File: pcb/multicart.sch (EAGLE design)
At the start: 16 parts, among them IC1 74HCT373N, IC3 27C08032P6, IC5 74HCT08N, Q1 BS170

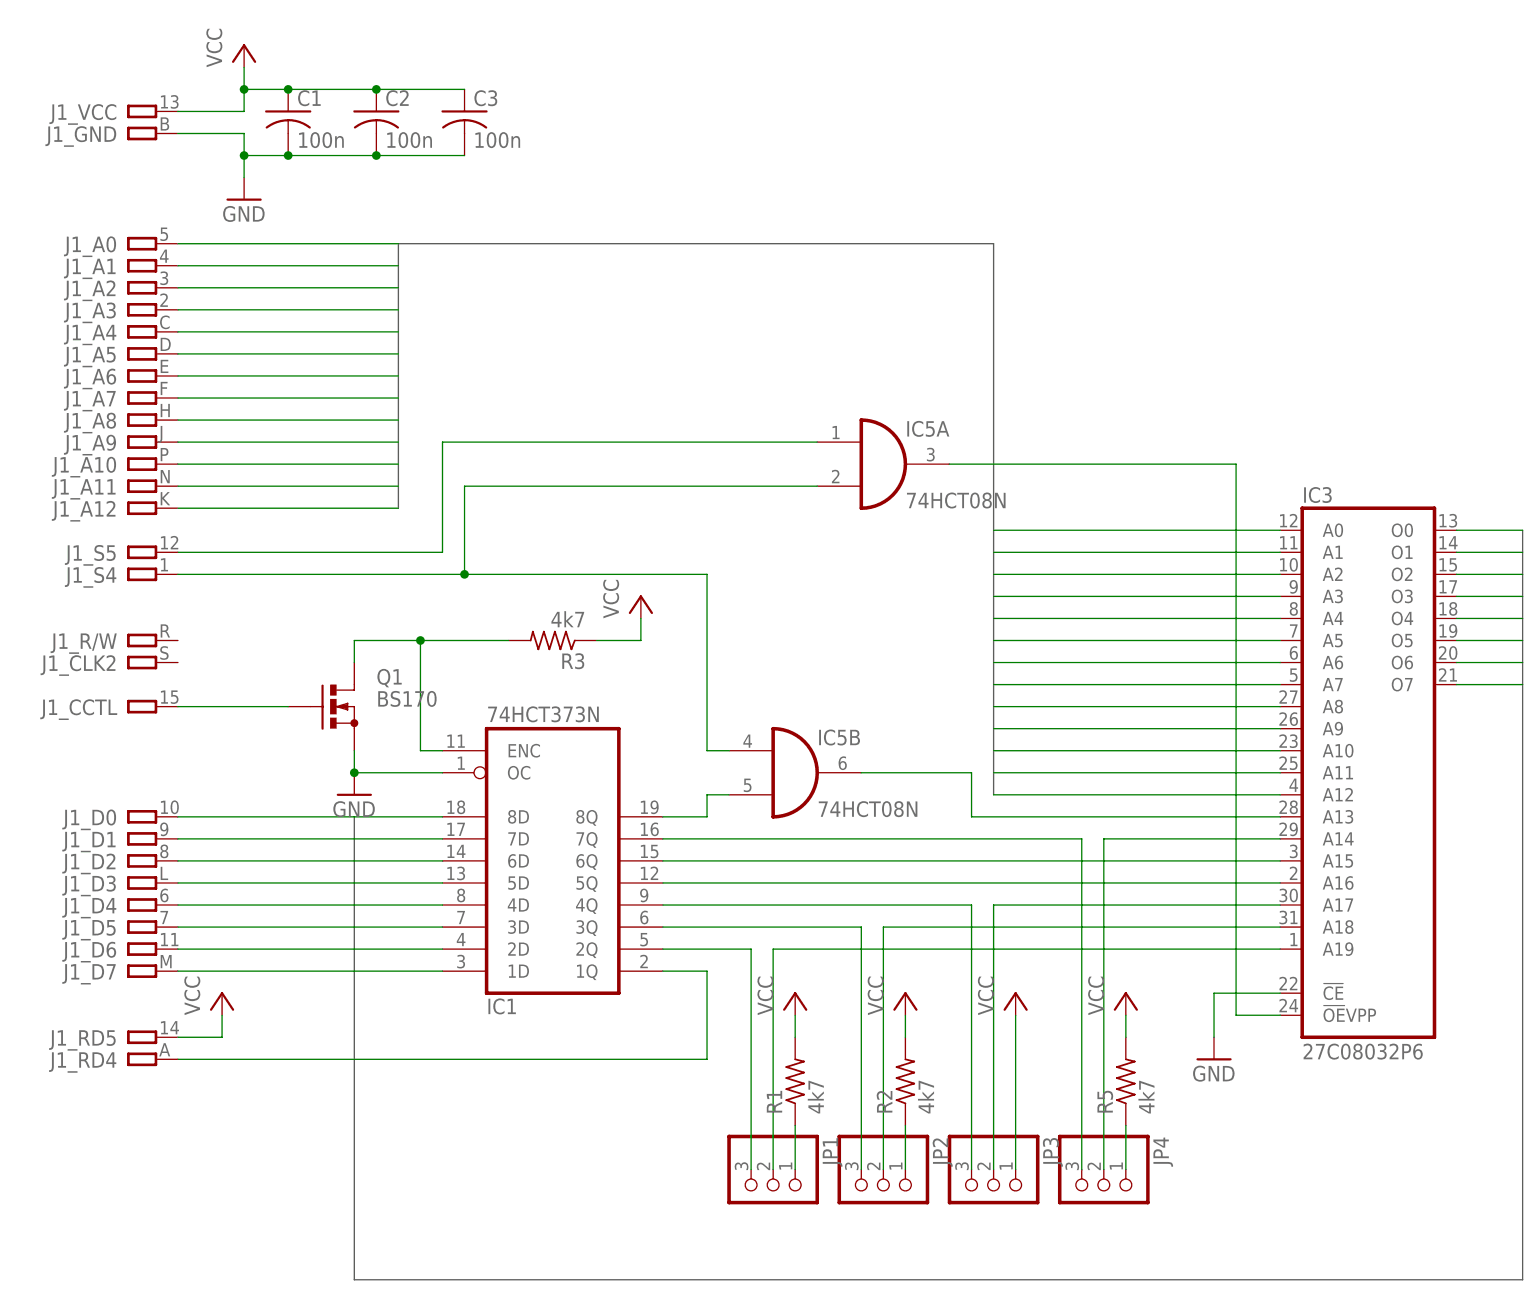
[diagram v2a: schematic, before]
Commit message: Optimized the PCB design.
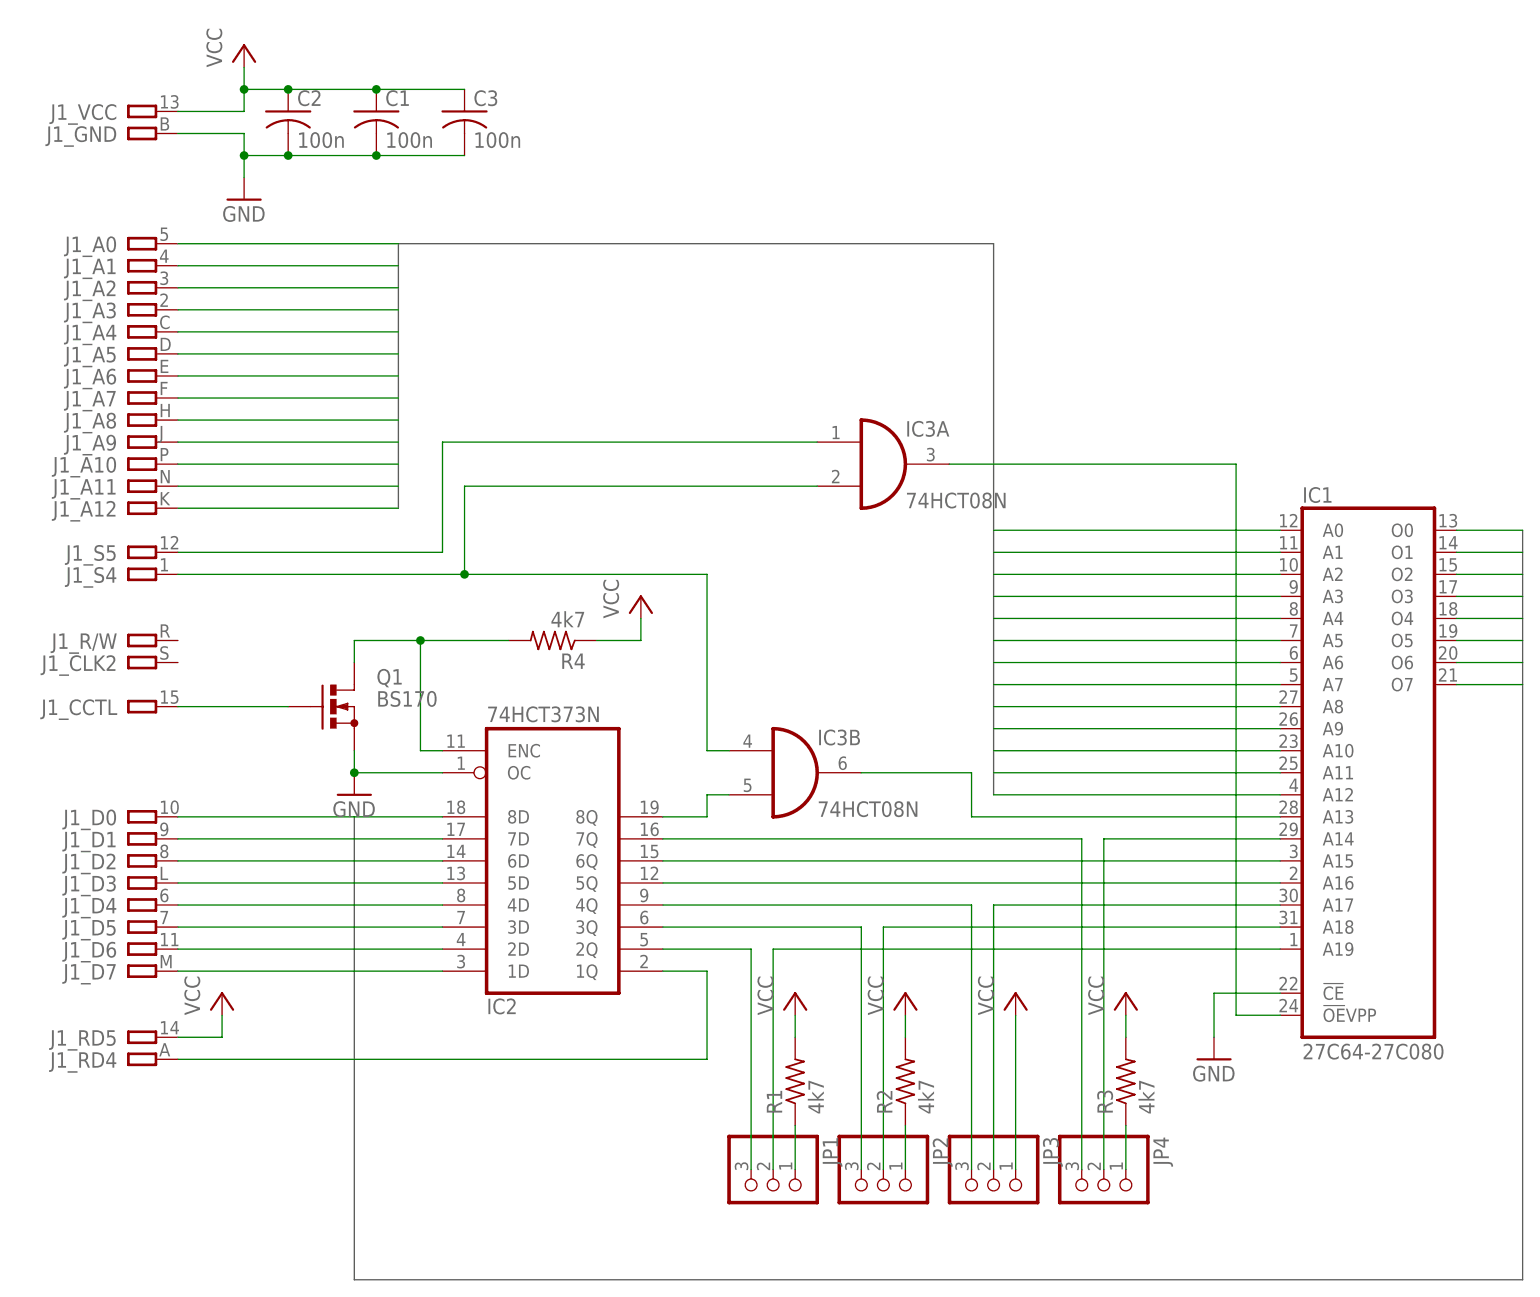
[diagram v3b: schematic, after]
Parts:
- removed IC5: 74HCT08N, 74xx-eu:74HCT08N
- removed R5: 4k7, resistor:R-US_0204/7
- added IC2: 74HCT373N, 74xx-eu:74HCT373N
- added R4: 4k7, resistor:R-US_0204/7
- IC1: value 74HCT373N -> 27C64-27C080; device 74xx-eu:74HCT373N -> atmel:27C08032P6
- IC3: value 27C08032P6 -> 74HCT08N; device atmel:27C08032P6 -> 74xx-eu:74HCT08N
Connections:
- net A0: now also IC1G$1.A0; no longer IC3G$1.A0
- net A1: now also IC1G$1.A1; no longer IC3G$1.A1
- net A10: now also IC1G$1.A10; no longer IC3G$1.A10
- net A11: now also IC1G$1.A11; no longer IC3G$1.A11
- net A12: now also IC1G$1.A12; no longer IC3G$1.A12
- net A2: now also IC1G$1.A2; no longer IC3G$1.A2
- net A3: now also IC1G$1.A3; no longer IC3G$1.A3
- net A4: now also IC1G$1.A4; no longer IC3G$1.A4
- net A5: now also IC1G$1.A5; no longer IC3G$1.A5
- net A6: now also IC1G$1.A6; no longer IC3G$1.A6
- net A7: now also IC1G$1.A7; no longer IC3G$1.A7
- net A8: now also IC1G$1.A8; no longer IC3G$1.A8
- net A9: now also IC1G$1.A9; no longer IC3G$1.A9
- net D0: now also IC1G$1.O0, IC2A.8D; no longer IC1A.8D, IC3G$1.O0
- net D1: now also IC1G$1.O1, IC2A.7D; no longer IC1A.7D, IC3G$1.O1
- net D2: now also IC1G$1.O2, IC2A.6D; no longer IC1A.6D, IC3G$1.O2
- net D3: now also IC1G$1.O3, IC2A.5D; no longer IC1A.5D, IC3G$1.O3
- net D4: now also IC1G$1.O4, IC2A.4D; no longer IC1A.4D, IC3G$1.O4
- net D5: now also IC1G$1.O5, IC2A.3D; no longer IC1A.3D, IC3G$1.O5
- net D6: now also IC1G$1.O6, IC2A.2D; no longer IC1A.2D, IC3G$1.O6
- net D7: now also IC1G$1.O7, IC2A.1D; no longer IC1A.1D, IC3G$1.O7
- net GND: now also IC1G$1.!CE, IC2A.OC; no longer IC1A.OC, IC3G$1.!CE
- net N$1: now also IC2A.8Q, IC3B.I1; no longer IC1A.8Q, IC5B.I1
- net N$10: now also IC1G$1.A18; no longer IC3G$1.A18
- net N$12: now also IC1G$1.A17; no longer IC3G$1.A17
- net N$13: now also IC1G$1.A19; no longer IC3G$1.A19
- net N$14: now also IC2A.2Q; no longer IC1A.2Q
- net N$15: now also IC1G$1.A14; no longer IC3G$1.A14
- net N$16: now also R3.1; no longer R5.1
- net N$18: now also IC3A.I0; no longer IC5A.I0
- net N$19: now also IC3A.I1, IC3B.I0; no longer IC5A.I1, IC5B.I0
- net N$2: now also IC2A.7Q; no longer IC1A.7Q
- net N$21: now also IC1G$1.A13, IC3B.O; no longer IC3G$1.A13, IC5B.O
- net N$22: now also IC2A.1Q; no longer IC1A.1Q
- net N$27: now also IC1G$1.!OE!VPP, IC3A.O; no longer IC3G$1.!OE!VPP, IC5A.O
- net N$3: now also IC1G$1.A15, IC2A.6Q; no longer IC1A.6Q, IC3G$1.A15
- net N$4: now also IC1G$1.A16, IC2A.5Q; no longer IC1A.5Q, IC3G$1.A16
- net N$5: now also IC2A.4Q; no longer IC1A.4Q
- net N$6: now also IC2A.3Q; no longer IC1A.3Q
- net N$7: now also IC2A.ENC, R4.2; no longer IC1A.ENC, R3.2
- net VCC: now also R3.2, R4.1; no longer R3.1, R5.2
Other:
- moved on the sheet: C1, C2, R3

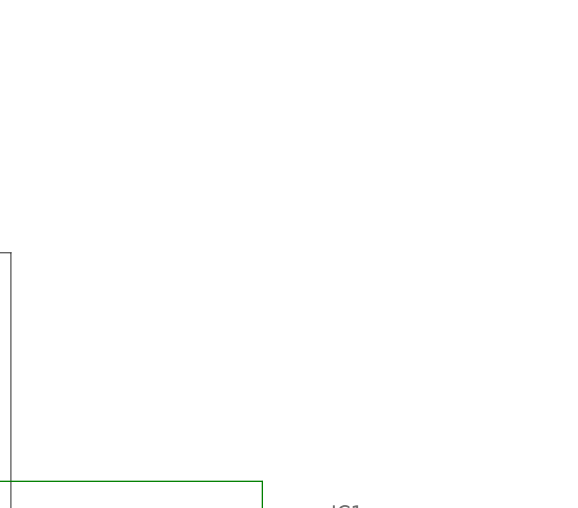
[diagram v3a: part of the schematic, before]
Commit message: Added OSHW logo to the PCB & the schematic.
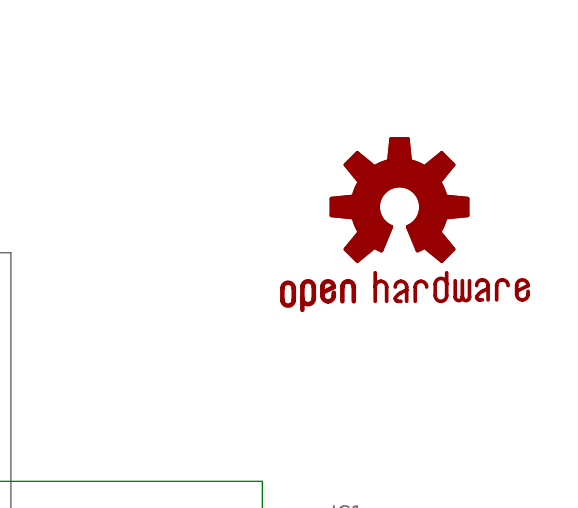
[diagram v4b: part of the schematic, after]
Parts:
- added GOLD_ORB_SM1: OSHWLOGO_GOLD_ORB_SM, bfl:OSHWLOGO_GOLD_ORB_SM
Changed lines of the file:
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@@
 <layer number="48" name="Document" color="7" fill="1" visible="no" active="no"/>
 <layer number="49" name="Reference" color="7" fill="1" visible="no" active="no"/>
+<layer number="50" name="dxf" color="7" fill="1" visible="no" active="no"/>
 <layer number="51" name="tDocu" color="7" fill="1" visible="no" active="no"/>
 <layer number="52" name="bDocu" color="7" fill="1" visible="no" active="no"/>
+<layer number="53" name="tGND_GNDA" color="7" fill="9" visible="no" active="no"/>
+<layer number="54" name="bGND_GNDA" color="1" fill="9" visible="no" active="no"/>
+<layer number="56" name="wert" color="7" fill="1" visible="no" active="no"/>
 <layer number="90" name="Modules" color="5" fill="1" visible="yes" active="yes"/>
 <layer number="91" name="Nets" color="2" fill="1" visible="yes" active="yes"/>
@@
 <layer number="98" name="Guide" color="6" fill="1" visible="yes" active="yes"/>
 <layer number="99" name="SpiceOrder" color="5" fill="1" visible="yes" active="yes"/>
+<layer number="100" name="Muster" color="7" fill="1" visible="no" active="no"/>
+<layer number="101" name="Patch_Top" color="12" fill="4" visible="yes" active="yes"/>
+<layer number="102" name="Vscore" color="7" fill="1" visible="yes" active="yes"/>
+<layer number="103" name="tMap" color="7" fill="1" visible="yes" active="yes"/>
+<layer number="104" name="Name" color="7" fill="1" visible="yes" active="yes"/>
+<layer number="105" name="tPlate" color="7" fill="1" visible="yes" active="yes"/>
+<layer number="106" name="bPlate" color="7" fill="1" visible="yes" active="yes"/>
+<layer number="107" name="Crop" color="7" fill="1" visible="yes" active="yes"/>
+<layer number="116" name="Patch_BOT" color="9" fill="4" visible="yes" active="yes"/>
+<layer number="121" name="_tsilk" color="7" fill="1" visible="yes" active="yes"/>
+<layer number="122" name="_bsilk" color="7" fill="1" visible="yes" active="yes"/>
+<layer number="125" name="_tNames" color="7" fill="1" visible="yes" active="yes"/>
+<layer number="144" name="Drill_legend" color="7" fill="1" visible="yes" active="yes"/>
+<layer number="151" name="HeatSink" color="7" fill="1" visible="yes" active="yes"/>
+<layer number="200" name="200bmp" color="1" fill="10" visible="yes" active="yes"/>
+<layer number="201" name="201bmp" color="2" fill="10" visible="yes" active="yes"/>
+<layer number="202" name="202bmp" color="3" fill="10" visible="yes" active="yes"/>
+<layer number="203" name="203bmp" color="4" fill="10" visible="yes" active="yes"/>
+<layer number="204" name="204bmp" color="5" fill="10" visible="yes" active="yes"/>
+<layer number="205" name="205bmp" color="6" fill="10" visible="yes" active="yes"/>
+<layer number="206" name="206bmp" color="7" fill="10" visible="yes" active="yes"/>
+<layer number="207" name="207bmp" color="8" fill="10" visible="yes" active="yes"/>
+<layer number="208" name="208bmp" color="9" fill="10" visible="yes" active="yes"/>
+<layer number="209" name="209bmp" color="7" fill="1" visible="yes" active="yes"/>
+<layer number="210" name="210bmp" color="7" fill="1" visible="yes" active="yes"/>
+<layer number="211" name="211bmp" color="7" fill="1" visible="yes" active="yes"/>
+<layer number="212" name="212bmp" color="7" fill="1" visible="yes" active="yes"/>
+<layer number="213" name="213bmp" color="7" fill="1" visible="yes" active="yes"/>
+<layer number="214" name="214bmp" color="7" fill="1" visible="yes" active="yes"/>
+<layer number="215" name="215bmp" color="7" fill="1" visible="yes" active="yes"/>
+<layer number="216" name="216bmp" color="7" fill="1" visible="yes" active="yes"/>
+<layer number="250" name="Descript" color="3" fill="1" visible="no" active="no"/>
+<layer number="251" name="SMDround" color="12" fill="11" visible="no" active="no"/>
+<layer number="254" name="cooling" color="7" fill="1" visible="yes" active="yes"/>
 </layers>
 <schematic xreflabel="%F%N/%S.%C%R" xrefpart="/%S.%C%R">
@@
 <part name="IC1" library="atmel" deviceset="27C080" device="32P6" value="27C64-27C080"/>
 <part name="JP1" library="pinhead" deviceset="PINHD-1X3" device=""/>
+<part name="GOLD_ORB_SM1" library="bfl" deviceset="OSHWLOGO" device="_GOLD_ORB_SM"/>
 </parts>
 <sheets>
@@
 <instance part="IC1" gate="G$1" x="134.62" y="53.34"/>
 <instance part="JP1" gate="A" x="66.04" y="5.08" rot="R270"/>
+<instance part="GOLD_ORB_SM1" gate="G$1" x="134.62" y="119.38"/>
 </instances>
 <busses>
